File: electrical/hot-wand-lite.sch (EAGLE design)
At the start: 107 parts, among them IC1 12V R-78K12-2.0, IC2 AMS1117-5.0, Q1 NCHAN, Q2 SIS862ADN-T1-GE3, Q3 SIS862ADN-T1-GE3, Q4 DMTH64M2LPDWQ-13, Q5 SIS862ADN-T1-GE3, Q6 2N7002K, Q7 G3404, SW1 SWITCH-SPDT-2MNT-SLW-864574-5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, U1 SEEED-XIAO-SAMD21-TH-LOCKING, U2 1EDN8511BXUSA1, U3 LM74810QDRRRQ1, U4 AP53781

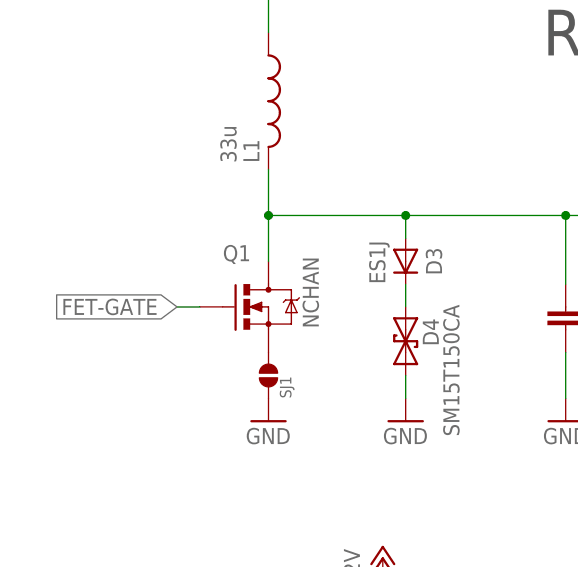
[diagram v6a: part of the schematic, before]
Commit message: net names changed for easier identification
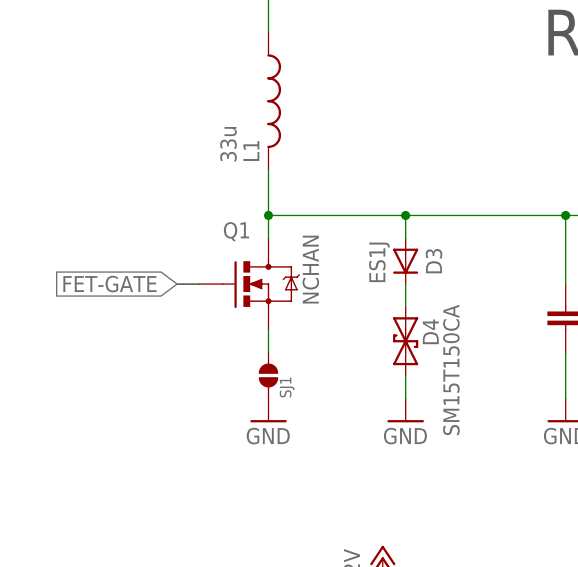
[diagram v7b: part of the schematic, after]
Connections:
- net N$1 renamed MOSFET-DRAIN
- net N$11 renamed MOSFET-SOURCE
- net N$12 renamed RF-RETURN
- net N$3 renamed M1
- net N$4 renamed M2
- net N$5 renamed M3
- net N$6 renamed M4
- net N$7 renamed RF-OUT
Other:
- moved on the sheet: Q1
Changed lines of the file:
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@@
 <attribute name="VALUE" x="186.944" y="-174.498" size="1.778" layer="96" rot="MR0"/>
 </instance>
-<instance part="Q1" gate="G$1" x="12.7" y="-190.5" smashed="yes">
-<attribute name="NAME" x="7.62" y="-185.42" size="1.778" layer="95"/>
-<attribute name="VALUE" x="16.51" y="-184.912" size="1.778" layer="96" rot="R270"/>
-<attribute name="JLC-DNP" x="12.7" y="-190.5" size="1.27" layer="96" display="off"/>
+<instance part="Q1" gate="G$1" x="12.7" y="-187.96" smashed="yes">
+<attribute name="NAME" x="7.62" y="-182.88" size="1.778" layer="95"/>
+<attribute name="VALUE" x="16.51" y="-182.372" size="1.778" layer="96" rot="R270"/>
+<attribute name="JLC-DNP" x="12.7" y="-187.96" size="1.27" layer="96" display="off"/>
 </instance>
 <instance part="F1" gate="G$1" x="203.2" y="-548.64">
@@
 <segment>
 <pinref part="Q1" gate="G$1" pin="G"/>
-<wire x1="5.08" y1="-190.5" x2="2.54" y2="-190.5" width="0.1524" layer="91"/>
-<label x="2.54" y="-190.5" size="1.778" layer="95" rot="R180" xref="yes"/>
+<wire x1="5.08" y1="-187.96" x2="2.54" y2="-187.96" width="0.1524" layer="91"/>
+<label x="2.54" y="-187.96" size="1.778" layer="95" rot="R180" xref="yes"/>
 </segment>
 </net>
@@
 </segment>
 </net>
-<net name="N$1" class="0">
+<net name="MOSFET-DRAIN" class="0">
 <segment>
 <pinref part="Q1" gate="G$1" pin="D"/>
@@
 <wire x1="12.7" y1="-175.26" x2="12.7" y2="-180.34" width="0.1524" layer="91"/>
 <pinref part="C2" gate="G$1" pin="1"/>
-<wire x1="12.7" y1="-180.34" x2="12.7" y2="-185.42" width="0.1524" layer="91"/>
+<wire x1="12.7" y1="-180.34" x2="12.7" y2="-182.88" width="0.1524" layer="91"/>
 <wire x1="12.7" y1="-180.34" x2="27.94" y2="-180.34" width="0.1524" layer="91"/>
 <pinref part="C1" gate="G$1" pin="1"/>
@@
 </segment>
 </net>
-<net name="N$3" class="0">
+<net name="M1" class="0">
 <segment>
 <pinref part="C2" gate="G$1" pin="2"/>
@@
 </segment>
 </net>
-<net name="N$4" class="0">
+<net name="M2" class="0">
 <segment>
 <pinref part="L2" gate="G$1" pin="2"/>
@@
 </segment>
 </net>
-<net name="N$5" class="0">
+<net name="M3" class="0">
 <segment>
 <pinref part="L3" gate="G$1" pin="2"/>
@@
 </segment>
 </net>
-<net name="N$6" class="0">
+<net name="M4" class="0">
 <segment>
 <pinref part="L4" gate="G$1" pin="2"/>
@@
 </segment>
 </net>
-<net name="N$7" class="0">
+<net name="RF-OUT" class="0">
 <segment>
 <pinref part="C10" gate="G$1" pin="1"/>
@@
 </segment>
 </net>
-<net name="N$11" class="0">
+<net name="MOSFET-SOURCE" class="0">
 <segment>
 <pinref part="Q1" gate="G$1" pin="S"/>
 <pinref part="SJ1" gate="A" pin="2"/>
-</segment>
-</net>
-<net name="N$12" class="0">
+<wire x1="12.7" y1="-193.04" x2="12.7" y2="-195.58" width="0.1524" layer="91"/>
+</segment>
+</net>
+<net name="RF-RETURN" class="0">
 <segment>
 <pinref part="JP1" gate="G$1" pin="2"/>

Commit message: lower voltage input limit for lite design
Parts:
- R30: value 56K -> 51K; JLCPARTNUM C23206 -> C23196
- R32: value 22K -> DNP; DNP (none) -> 1; JLCPARTNUM C31850 -> (none)
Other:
- note added: "OV cutoff: 32.6 V nominal, 31.1 V to 34.2 V worst-case"
- note added: "VDS(peak) ~= 3.56 x Vin"
- note removed: "OV cutoff: 38.8 V nominal, 37.0 V to 40.8 V worst-case"
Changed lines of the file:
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@@
 <attribute name="JLCPARTNUM" value="C14663"/>
 </part>
-<part name="R30" library="hot-wand" deviceset="RESISTOR" device="0603-RES" value="56K">
-<attribute name="JLCPARTNUM" value="C23206"/>
+<part name="R30" library="hot-wand" deviceset="RESISTOR" device="0603-RES" value="51K">
+<attribute name="JLCPARTNUM" value="C23196"/>
 </part>
 <part name="C26" library="hot-wand" deviceset="CAP" device="0603-CAP" value="100n">
 <attribute name="JLCPARTNUM" value="C14663"/>
 </part>
-<part name="R32" library="hot-wand" deviceset="RESISTOR" device="0603-RES" value="22K">
-<attribute name="JLCPARTNUM" value="C31850"/>
+<part name="R32" library="hot-wand" deviceset="RESISTOR" device="0603-RES" value="DNP">
+<attribute name="DNP" value="1"/>
 </part>
 <part name="R31" library="hot-wand" deviceset="RESISTOR" device="0603-RES" value="2K">
@@
 <text x="138.176" y="-494.538" size="1.016" layer="97">50V each</text>
 <text x="138.176" y="-481.838" size="1.016" layer="97">inrush ~1A/30ms</text>
-<text x="149.86" y="-508" size="1.27" layer="97">OV cutoff: 38.8 V nominal, 37.0 V to 40.8 V worst-case</text>
+<text x="149.86" y="-508" size="1.27" layer="97">OV cutoff: 32.6 V nominal, 31.1 V to 34.2 V worst-case</text>
 <text x="165.1" y="-541.02" size="1.27" layer="97">this protects the AP53781
 from high battery voltage</text>
+<text x="15.24" y="-177.8" size="1.016" layer="97">VDS(peak) ~= 3.56 x Vin</text>
 </plain>
 <instances>
